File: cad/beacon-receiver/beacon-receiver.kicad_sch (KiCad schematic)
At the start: 12 parts, among them J1 STEP-MXO2 IF, J2 PD cable, U1 MCP6022 (TIA; U1B unused), U2 MCP3201

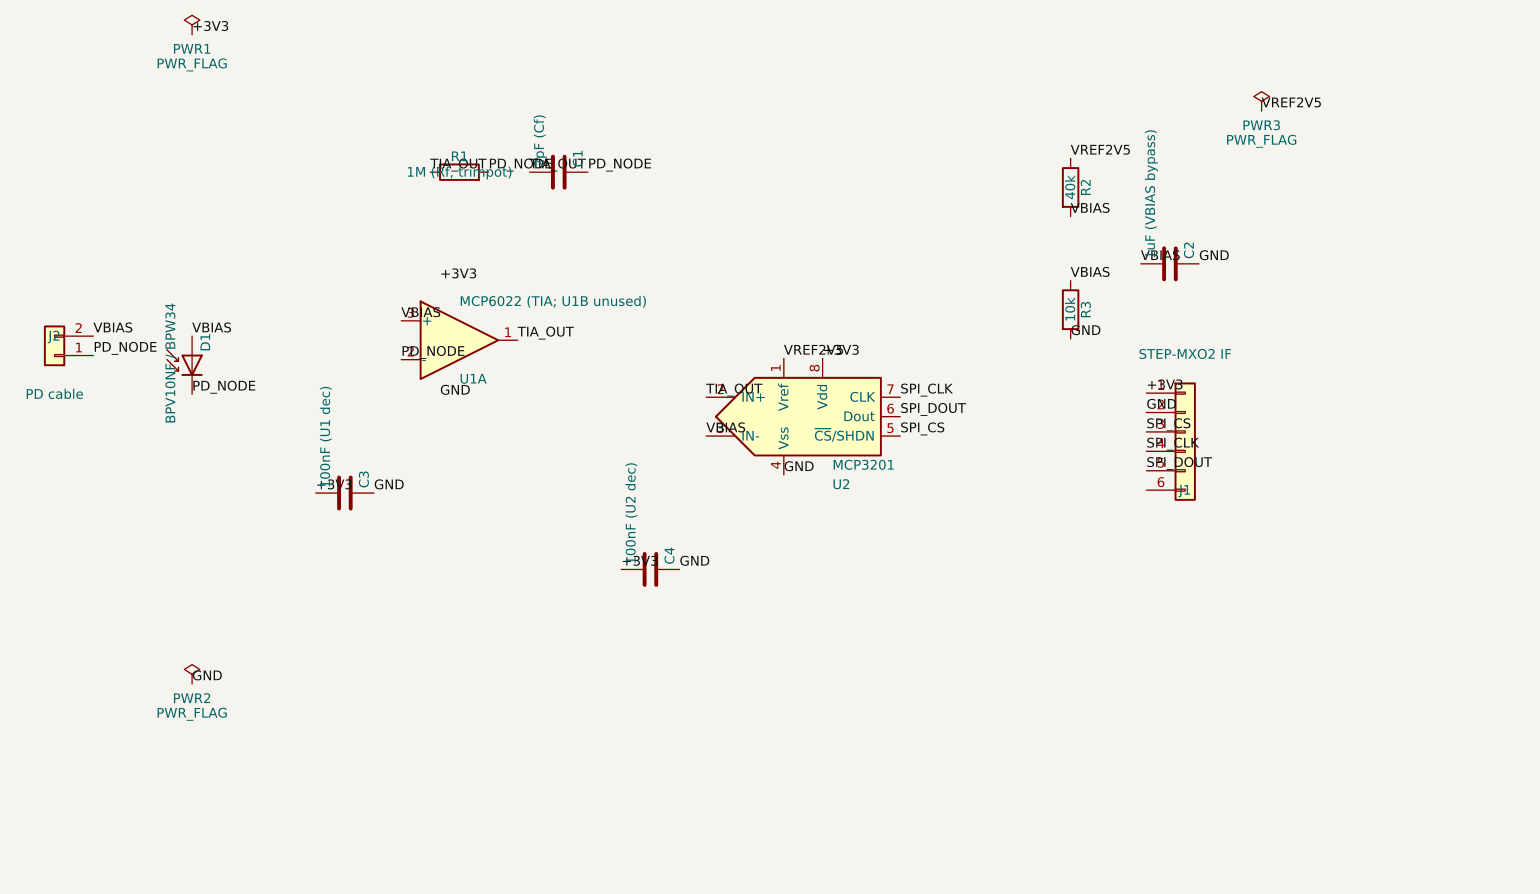
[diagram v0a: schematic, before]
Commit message: checkpoint(031): receiver schematic + 200 Hz sim + speckit re-scope (camera → 040)
- Receiver schematic (cad/beacon-receiver): KiCad capture cleaned up in GUI — D1 PD
  (cathode→PD_NODE / anode→VBIAS), MCP6022 TIA (unit A + tied-off B + power C),
  MCP1525 2.5V ref → VREF2V5, R2/R3 VBIAS divider + bypass, MCP3201 ADC (IN−→GND),
  J1→STEP-MXO2 SPI mapping. ERC 0. PDF refreshed; SVG + TODO dropped.
- Acquisition sim → 200 Hz chip rate (480 fps / 2.4 fpc); results + plots regenerated
  (full 15-chip code now 75 ms = 1.5 ticks @ 20 Hz). Research plan section 7/8 updated.
- Speckit re-scope: 031 = 1-bit single-IR-sensor acquisition phase (active = Phase A in
  tasks.md); the full camera pipeline split out to a new feature 040 (camera redo,
  emitters shared). Banners in spec.md/plan.md/tasks.md/acquisition-research-plan.md.
- BACKLOG: re-homed the camera-front-end + perception/FOV items to 040; added the
  two-component physical CEP model (decode-confidence + apparent-motion) for a cleaner
  tracker-mode first pass.
- Cleanup: emitter schematic PNG removed (keep PDF); repointed the .png references.

Co-Authored-By: Claude Opus 4.8 (1M context) <noreply@anthropic.com>
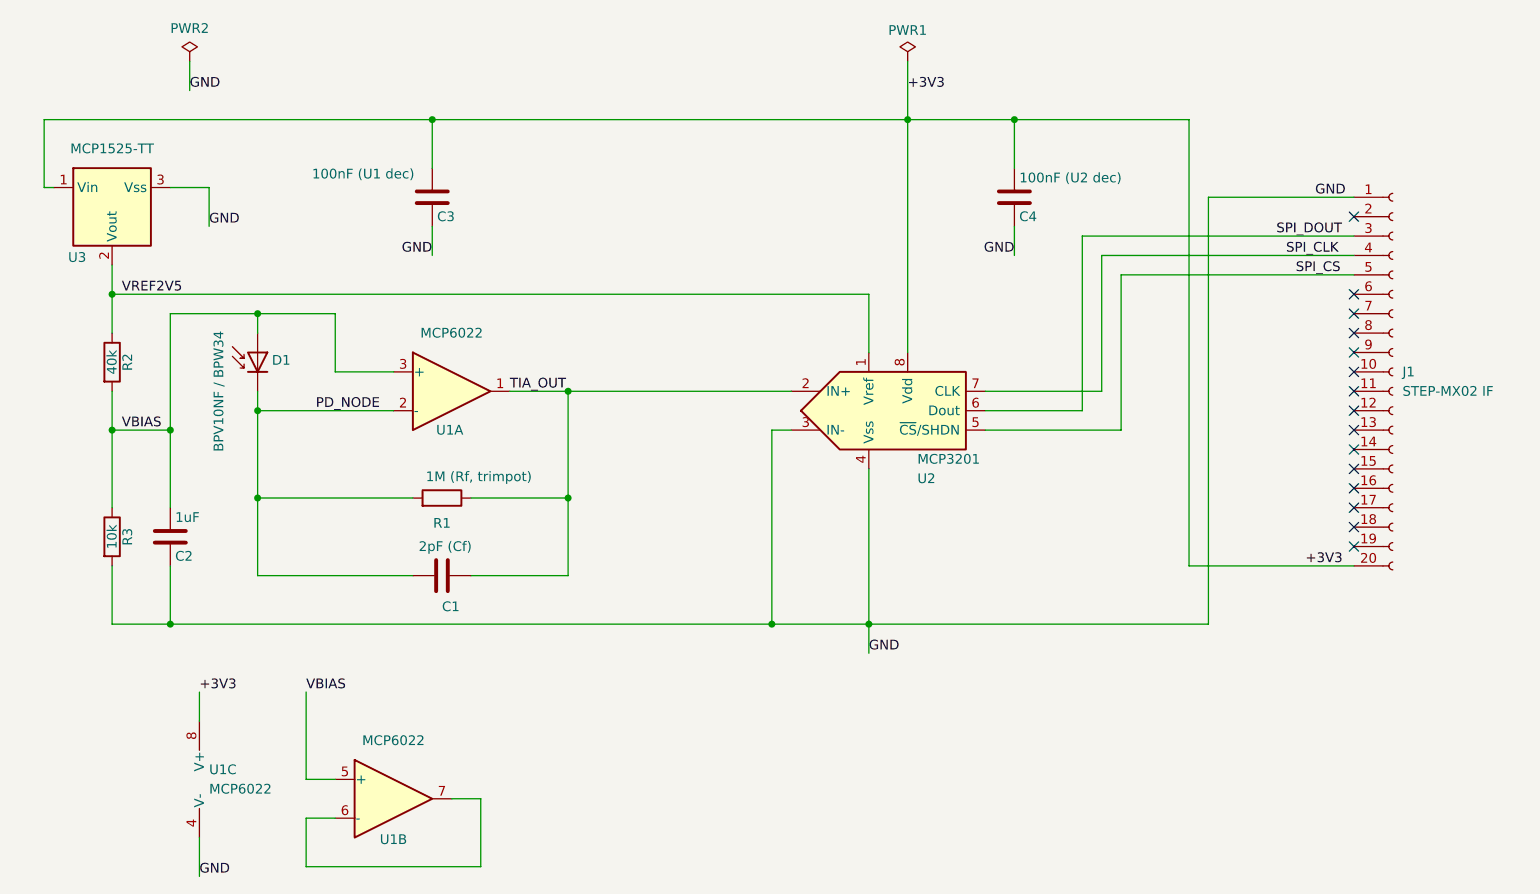
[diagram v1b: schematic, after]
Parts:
- removed J1: STEP-MXO2 IF, symbol Connector_Generic:Conn_01x06
- removed J2: PD cable, symbol Connector_Generic:Conn_01x02
- added J1: STEP-MX02 IF, symbol Connector:Conn_01x20_Socket
- added unit 2 of U1
- added U3: MCP1525-TT, Package_TO_SOT_SMD:SOT-23, symbol Reference_Voltage:MCP1525-TT
- C2: value 1uF (VBIAS bypass) -> 1uF
- U1: value MCP6022 (TIA; U1B unused) -> MCP6022
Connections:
- net +3V3: now also J1.20 (Pin_20), U1.8 (V+), U3.1 (Vin)
- net GND: now also U2.3 (IN-), J1.1 (Pin_1), U1.4 (V-), U3.3 (Vss)
- net SPI_CLK: now also J1.4 (Pin_4)
- net SPI_CS: now also J1.5 (Pin_5)
- net SPI_DOUT: now also J1.3 (Pin_3)
- net VBIAS: now also U1.5 (+); no longer U2.3 (IN-)
- net VREF2V5: now also U3.2 (Vout)
- new net: U1.6 (-), U1.7
- no-connect marks 0 -> 15
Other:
- moved on the sheet: C1, C2, C3, C4, D1, R1, R2, R3, U2
